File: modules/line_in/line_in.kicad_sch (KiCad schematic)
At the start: 24 parts, among them J1 AudioJack3, J2 Outputs, U1 LM358, U2 LM358, U3 LM358

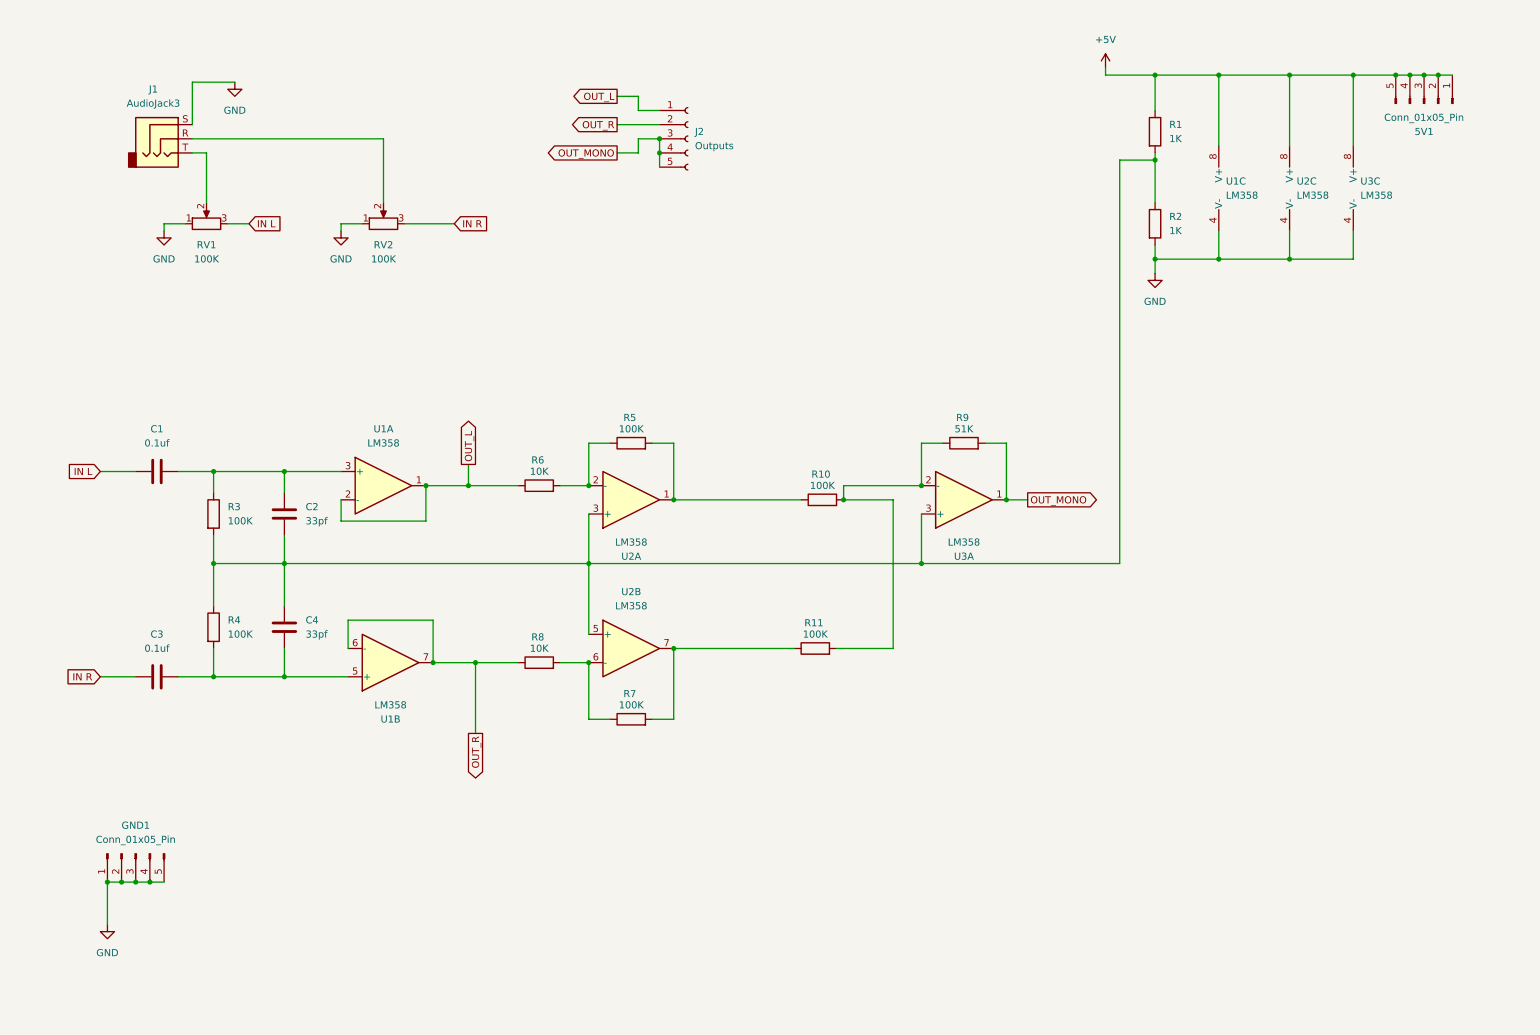
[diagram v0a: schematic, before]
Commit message: Add the schematic for the PCB
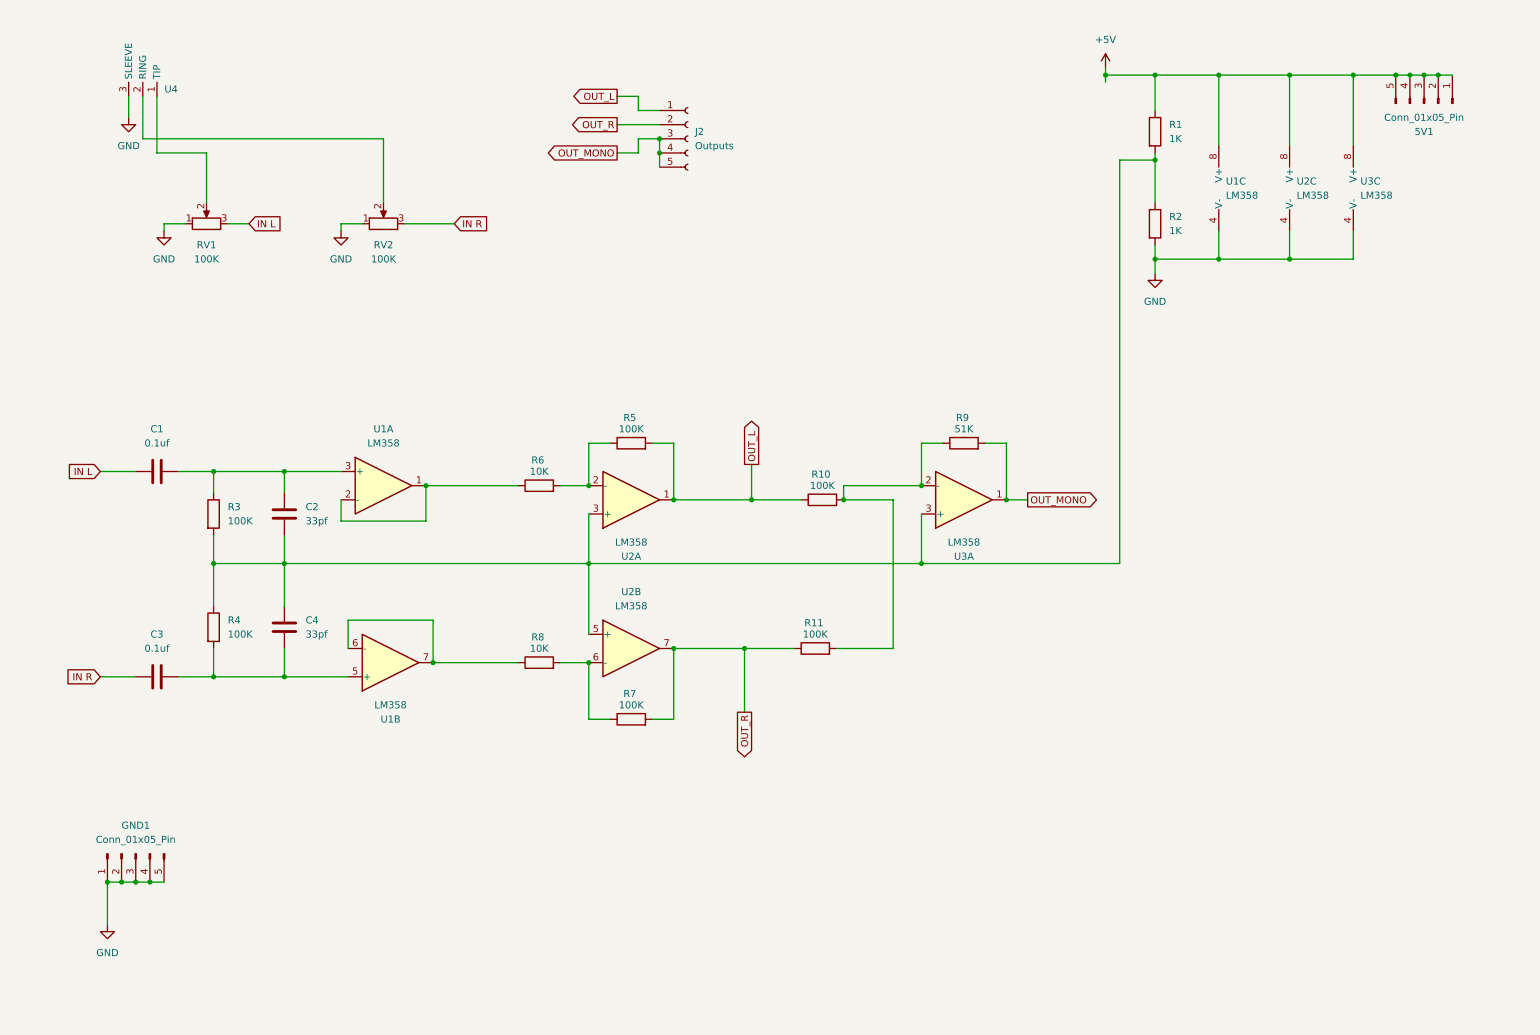
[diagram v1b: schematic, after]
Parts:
- removed J1: AudioJack3, symbol Connector_Audio:AudioJack3
- added U4: ~, Footprints:Audio_Socket_TRS_3.5mm, symbol Symbols:Audio_Jack_TRS_3.5mm
- C1, C2, C3, C4: footprint (none) -> Capacitor_SMD:C_0402_1005Metric
- J2: footprint (none) -> Connector_PinSocket_2.54mm:PinSocket_1x05_P2.54mm_Vertical
- R1, R10, R11, R2, R3, R4, R5, R6, R7, R8, R9: footprint (none) -> Resistor_SMD:R_0402_1005Metric
- RV1, RV2: footprint (none) -> Potentiometer_THT:Potentiometer_Alpha_RD901F-40-00D_Single_Vertical
- U1, U2, U3: footprint (none) -> Package_SO:SOIC-8-1EP_3.9x4.9mm_P1.27mm_EP2.29x3mm
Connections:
- net GND: now also U4.3 (SLEEVE)
- net OUT_L: now also R10.1, R5.2, U2.1; no longer R6.1, U1.1, U1.2 (-)
- net OUT_R: now also R11.1, R7.2, U2.7; no longer R8.1, U1.6 (-), U1.7
- net at RV2.2: now also U4.2 (RING)
- net at RV1.2: now also U4.1 (TIP)
- new net: R6.1, U1.1, U1.2 (-)
- new net: R8.1, U1.6 (-), U1.7

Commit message: Make sure SMD via are not placed on pads.
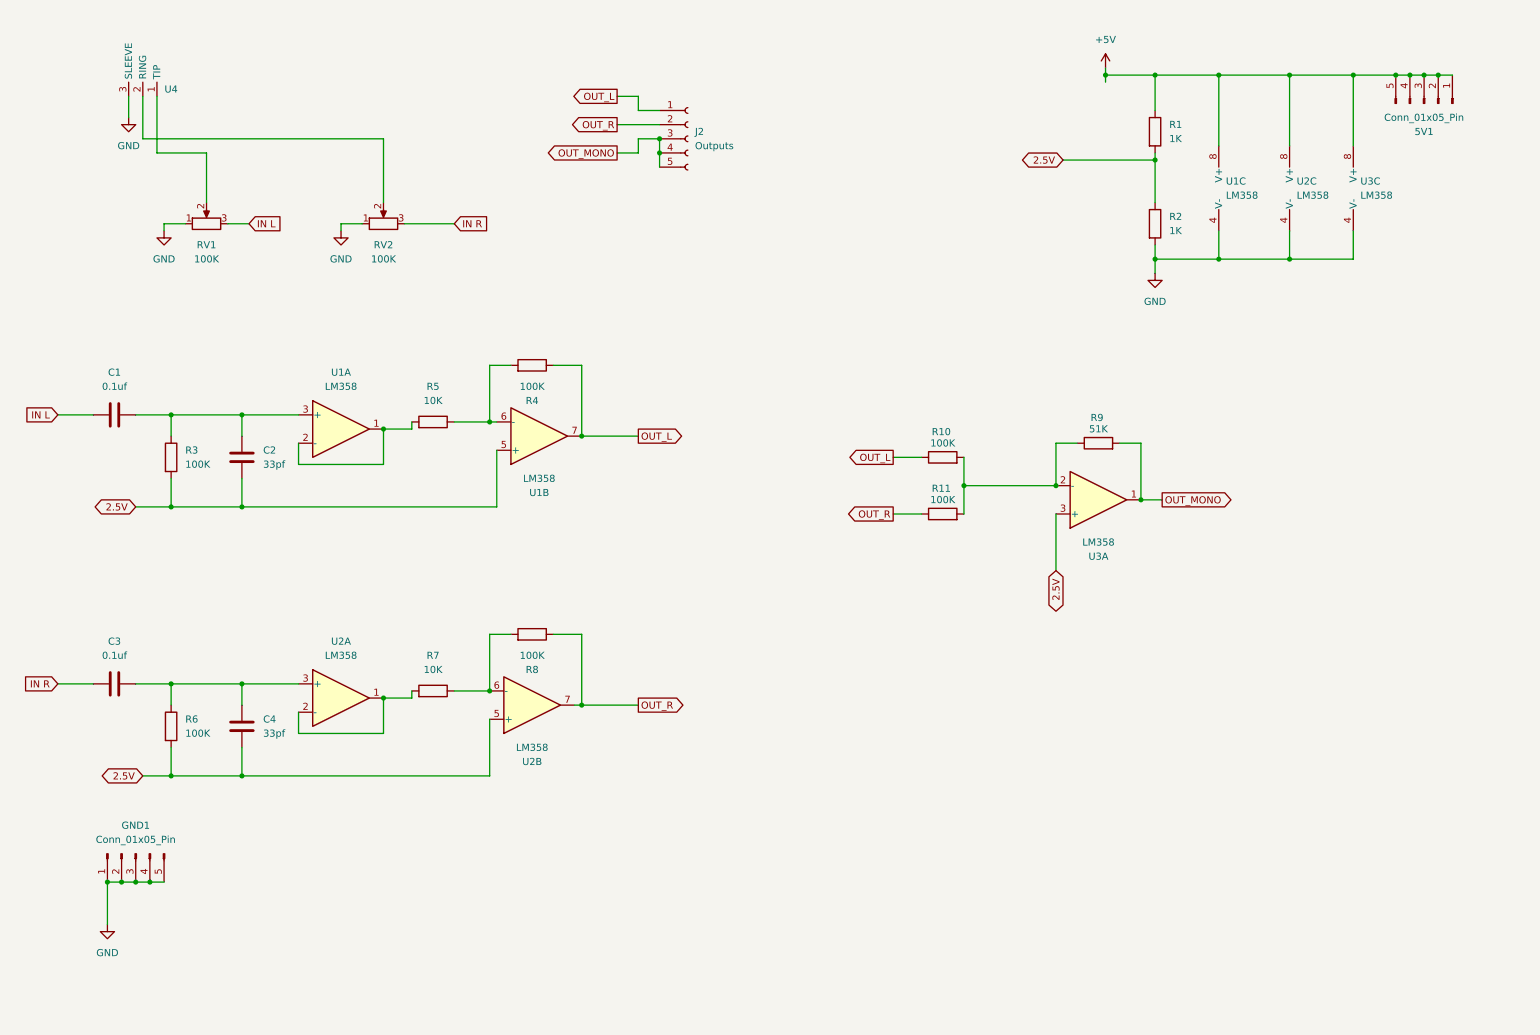
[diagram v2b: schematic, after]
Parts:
- R5, R7: value 100K -> 10K
- R6, R8: value 10K -> 100K
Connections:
- net OUT_L: now also R4.1, U1.7; no longer R5.2, U2.1
- net OUT_R: now also R8.1; no longer R7.2
- net 2.5V: now reaches C2.2, R1.2, R2.1, R3.2, U2.5 (+), U3.3 (+)
- net 2.5V: now also C4.2, R6.2, U1.5 (+); no longer C4.1, R4.1, U2.3 (+)
- net at U1.1, U1.2 (-): now also R5.2; no longer R6.1
- new net: R4.2, R5.1, U1.6 (-)
- new net: C3.1, C4.1, R6.1, U2.3 (+)
- new net: R7.2, U2.1, U2.2 (-)
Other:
- moved on the sheet: C1, C2, R10, R11, R3, R9, U1A, U1B, U3A

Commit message: Start working on the new version of line_in
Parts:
- removed C3: 0.1uf, Capacitor_SMD:C_0402_1005Metric, symbol Device:C
- removed C4: 33pf, Capacitor_SMD:C_0402_1005Metric, symbol Device:C
- removed J2: Outputs, Connector_PinSocket_2.54mm:PinSocket_1x05_P2.54mm_Vertical, symbol Connector:Conn_01x05_Socket
- removed R10, R11, R6, R8: 100K, Resistor_SMD:R_0402_1005Metric, symbol Device:R
- removed R7: 10K, Resistor_SMD:R_0402_1005Metric, symbol Device:R
- removed R9: 51K, Resistor_SMD:R_0402_1005Metric, symbol Device:R
- removed RV2: 100K, Potentiometer_THT:Potentiometer_Alpha_RD901F-40-00D_Single_Vertical, symbol Device:R_Potentiometer
- removed U2, U3: LM358, Package_SO:SOIC-8-1EP_3.9x4.9mm_P1.27mm_EP2.29x3mm, symbol Amplifier_Operational:LM358
- removed U4: ~, Footprints:Audio_Socket_TRS_3.5mm, symbol Symbols:Audio_Jack_TRS_3.5mm
- added INPUT1, OUTPUT2: Conn_01x05_Socket, Connector_PinSocket_2.54mm:PinSocket_1x05_P2.54mm_Vertical, symbol Connector:Conn_01x05_Socket
- added V1: 5, symbol Simulation_SPICE:VDC
- added V2: VSIN, symbol Simulation_SPICE:VSIN
- C1: footprint Capacitor_SMD:C_0402_1005Metric -> (none)
- C2: value 33pf -> 0.1uf; footprint Capacitor_SMD:C_0402_1005Metric -> (none)
- R1, R2: value 1K -> 1k; footprint Resistor_SMD:R_0402_1005Metric -> (none)
- R3: value 100K -> 100k; footprint Resistor_SMD:R_0402_1005Metric -> (none)
- R4: value 100K -> 24k; footprint Resistor_SMD:R_0402_1005Metric -> (none)
- R5: value 10K -> 100k; footprint Resistor_SMD:R_0402_1005Metric -> (none)
- RV1: value 100K -> 50k; footprint Potentiometer_THT:Potentiometer_Alpha_RD901F-40-00D_Single_Vertical -> (none)
- U1: footprint Package_SO:SOIC-8-1EP_3.9x4.9mm_P1.27mm_EP2.29x3mm -> (none)
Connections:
- net +5V: now also C1.1, V1.1
- net 2.5V: now also C1.2, R5.2; no longer C2.2, R3.2
- net GND: now also V1.2, V2.2
- net OUT_L: now also R3.2; no longer R4.1
- net at R4.2, U1.6 (-): now also R3.1; no longer R5.1
- net at U1.1, U1.2 (-): now also R4.1; no longer R5.2
- net at RV1.2: now also C2.1
- net IN L renamed IN_L
- net IN_L: now also V2.1; no longer C1.2
- new net: C2.2, R5.1, U1.3 (+)
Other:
- moved on the sheet: 5V1, GND1

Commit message: Finalize the core design
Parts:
- removed INPUT1: Conn_01x05_Socket, Connector_PinSocket_2.54mm:PinSocket_1x05_P2.54mm_Vertical, symbol Connector:Conn_01x05_Socket
- added C3, C4, C6: 0.1uf, symbol Device:C
- added C5: 0.01uf, symbol Device:C
- added R10, R12, R6, R8: 100k, symbol Device:R
- added R11: 1k, symbol Device:R
- added R7: 24k, symbol Device:R
- added R9: 50k, symbol Device:R
- added RV2: 50k, symbol Device:R_Potentiometer
- added U2, U3: LM358, symbol Amplifier_Operational:LM358
- added V3: VSIN, symbol Simulation_SPICE:VSIN
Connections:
- net +5V: now also C4.1, C6.1, U2.8 (V+), U3.8 (V+)
- net 2.5V: now also C4.2, C6.2, R6.2, U2.5 (+), U3.3 (+)
- net GND: now also C5.2, RV2.1, U2.4 (V-), U3.4 (V-), V3.2
- net OUT_L: now also OUTPUT2.1 (Pin_1), R10.1
- net OUT_R: now reaches OUTPUT2.2 (Pin_2)
- net OUT_R: now also R12.1, R8.2, U2.7
- net OUT_MONO: now reaches OUTPUT2.3 (Pin_3)
- net OUT_MONO: now also OUTPUT2.4 (Pin_4), OUTPUT2.5 (Pin_5), C5.1, R11.2
- new net: R10.2, R12.2, R9.1, U3.2 (-)
- new net: C3.2, R6.1, U2.3 (+)
- new net: R11.1, R9.2, U3.1
- new net: R7.2, R8.1, U2.6 (-)
- new net: C3.1, RV2.2
- new net: R7.1, U2.1, U2.2 (-)
- new net IN_R: RV2.3, V3.1
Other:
- moved on the sheet: C1, C2, R3, R4, R5, RV1, U1A, U1B, U1C

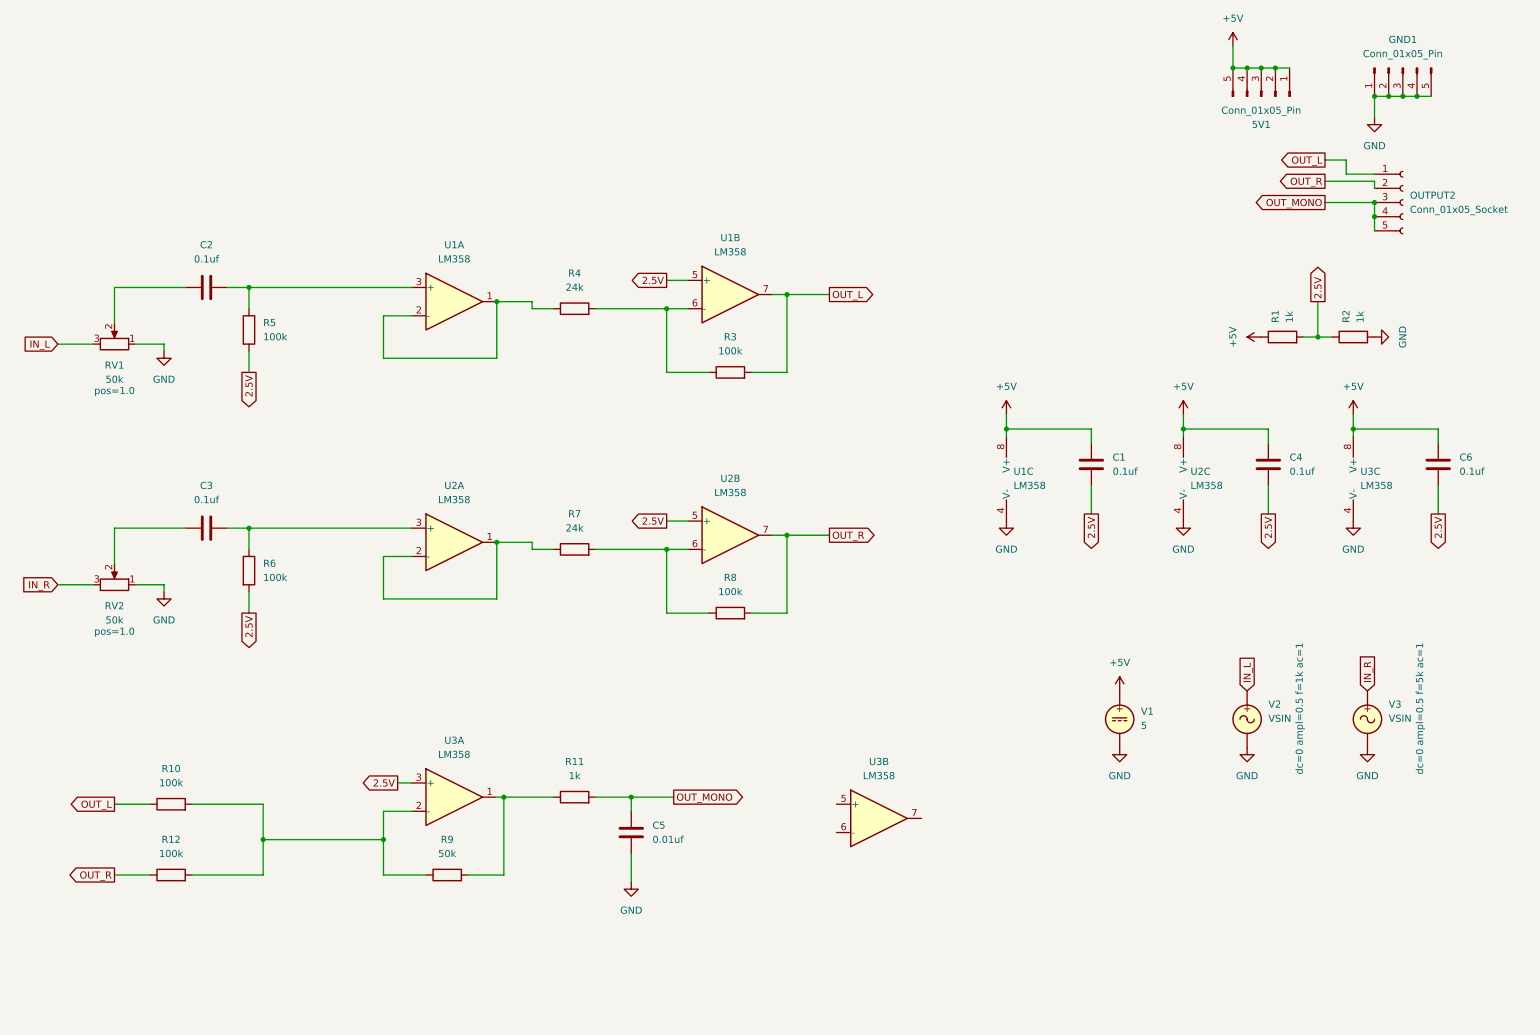
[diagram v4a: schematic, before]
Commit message: Add AudioJacks submodule with KiCad footprints.
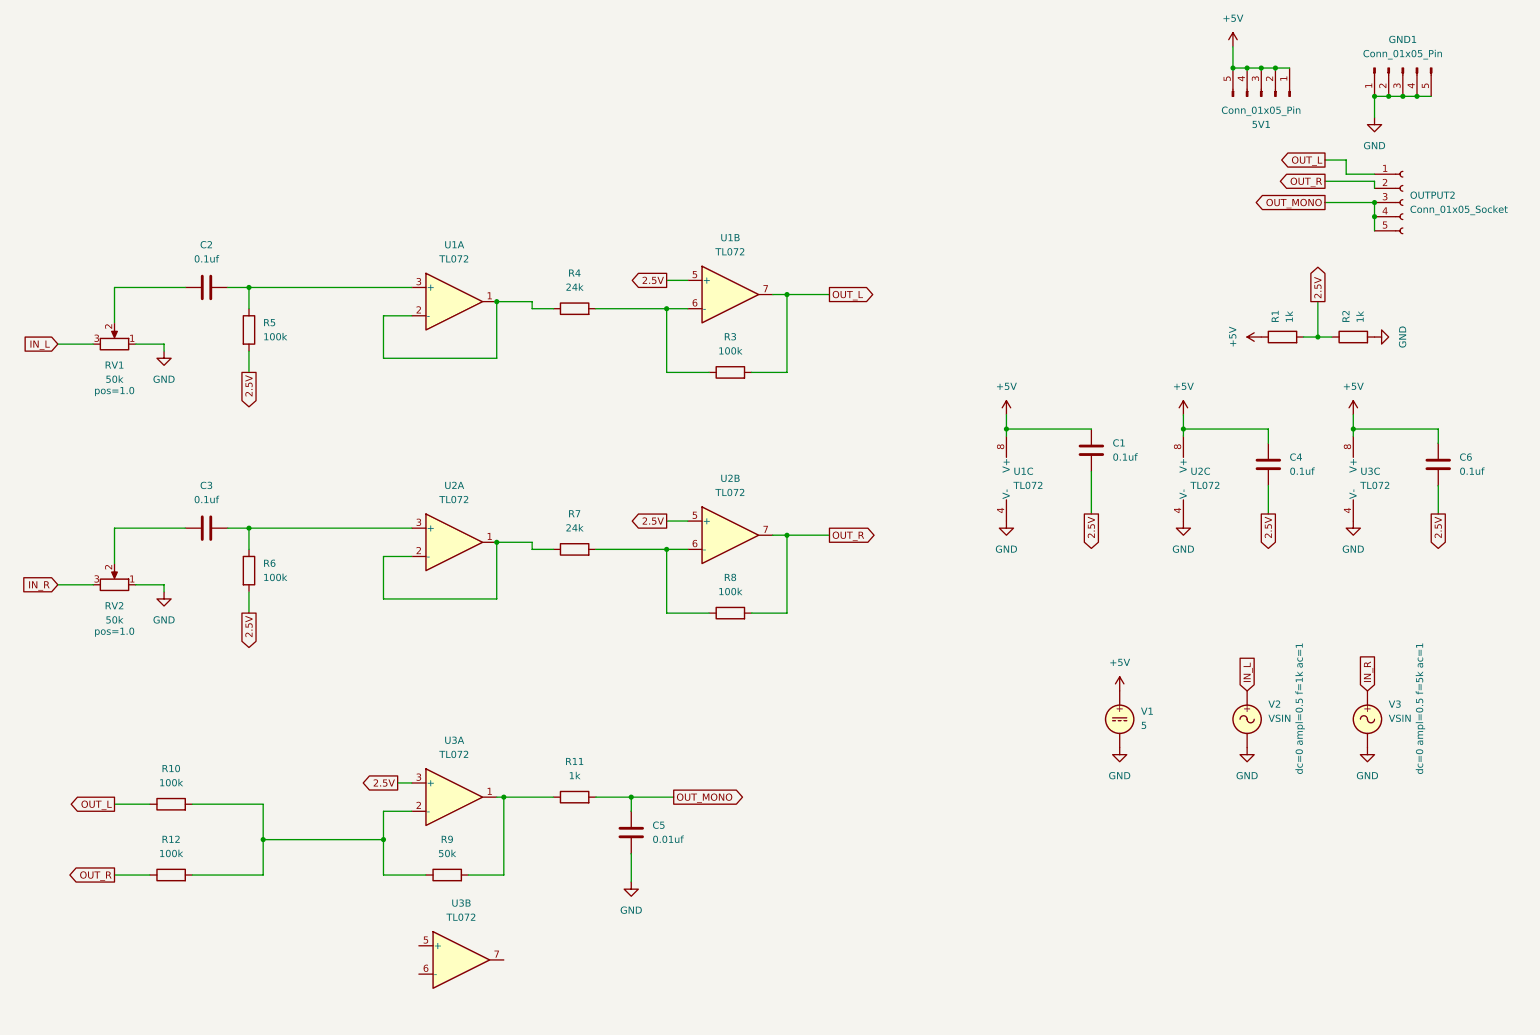
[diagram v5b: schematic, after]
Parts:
- removed U1, U2, U3: LM358, symbol Amplifier_Operational:LM358
- added U1, U2, U3: TL072, symbol Amplifier_Operational:TL072
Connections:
- net +5V: now also U1.8 (V+), U2.8 (V+), U3.8 (V+)
- net 2.5V: now also U1.5 (+), U2.5 (+), U3.3 (+)
- net GND: now also U1.4 (V-), U2.4 (V-), U3.4 (V-)
- net OUT_L: now also U1.7
- net OUT_R: now also U2.7
- net at R10.2, R12.2, R9.1: now also U3.2 (-)
- net at R3.1, R4.2: now also U1.6 (-)
- net at C3.2, R6.1: now also U2.3 (+)
- net at R11.1, R9.2: now also U3.1
- net at R7.2, R8.1: now also U2.6 (-)
- net at C2.2, R5.1: now also U1.3 (+)
- net at R4.1: now also U1.1, U1.2 (-)
- net at R7.1: now also U2.1, U2.2 (-)
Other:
- moved on the sheet: C1

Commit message: Finalize the schematic design
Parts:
- removed C1, C4, C6: 0.1uf, symbol Device:C
- added C7, C8, C9: 0.1uf, symbol Device:C
- added J1: AudioJack3, BreadModular_AudioJacks:Jack_3.5mm_QingPu_WQP-PJ366ST_Vertical, symbol Connector_Audio:AudioJack3
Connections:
- net 2.5V: now also C7.2, C8.2, C9.2
- net GND: now also C7.1, C8.1, C9.1, J1.S
- net IN_L: now also J1.T
- net IN_R: now also J1.R
